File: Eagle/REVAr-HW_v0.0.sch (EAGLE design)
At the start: 74 parts, among them IC1 MC33269ST-5.0T3, IC2 MC33269D-5.0, IC3 ATMEGA2560-16AU, IC4 ATMEGA8U2-MU, IC5 LM358D, IC6 LP2985-33DBVR, Q1 16MHz, Q2 16MHz, T2 FDN340P, X1 DC21MMX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

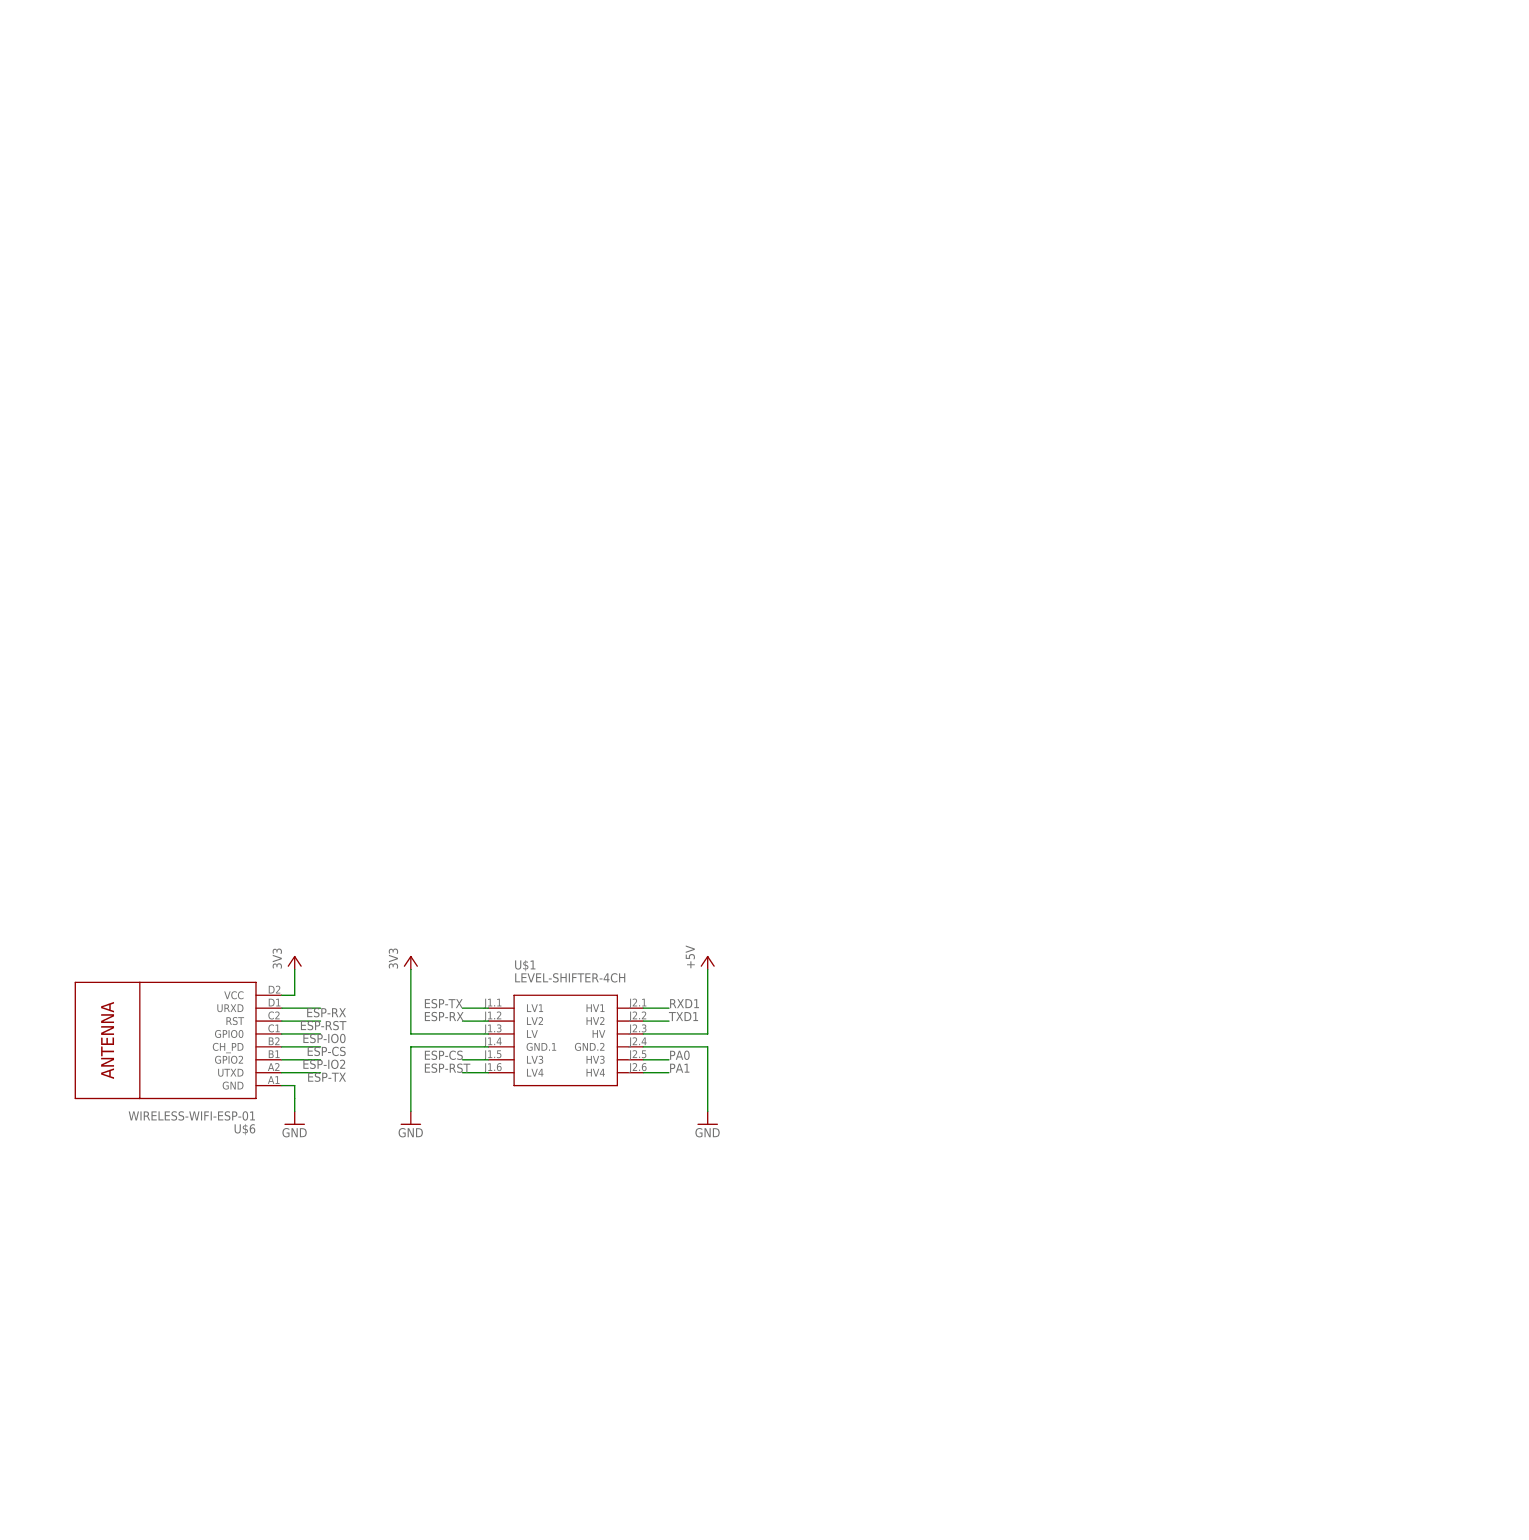
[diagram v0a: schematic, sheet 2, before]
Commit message: [HW] Add SPEC gas sensors and communication via RS485 with Arduino
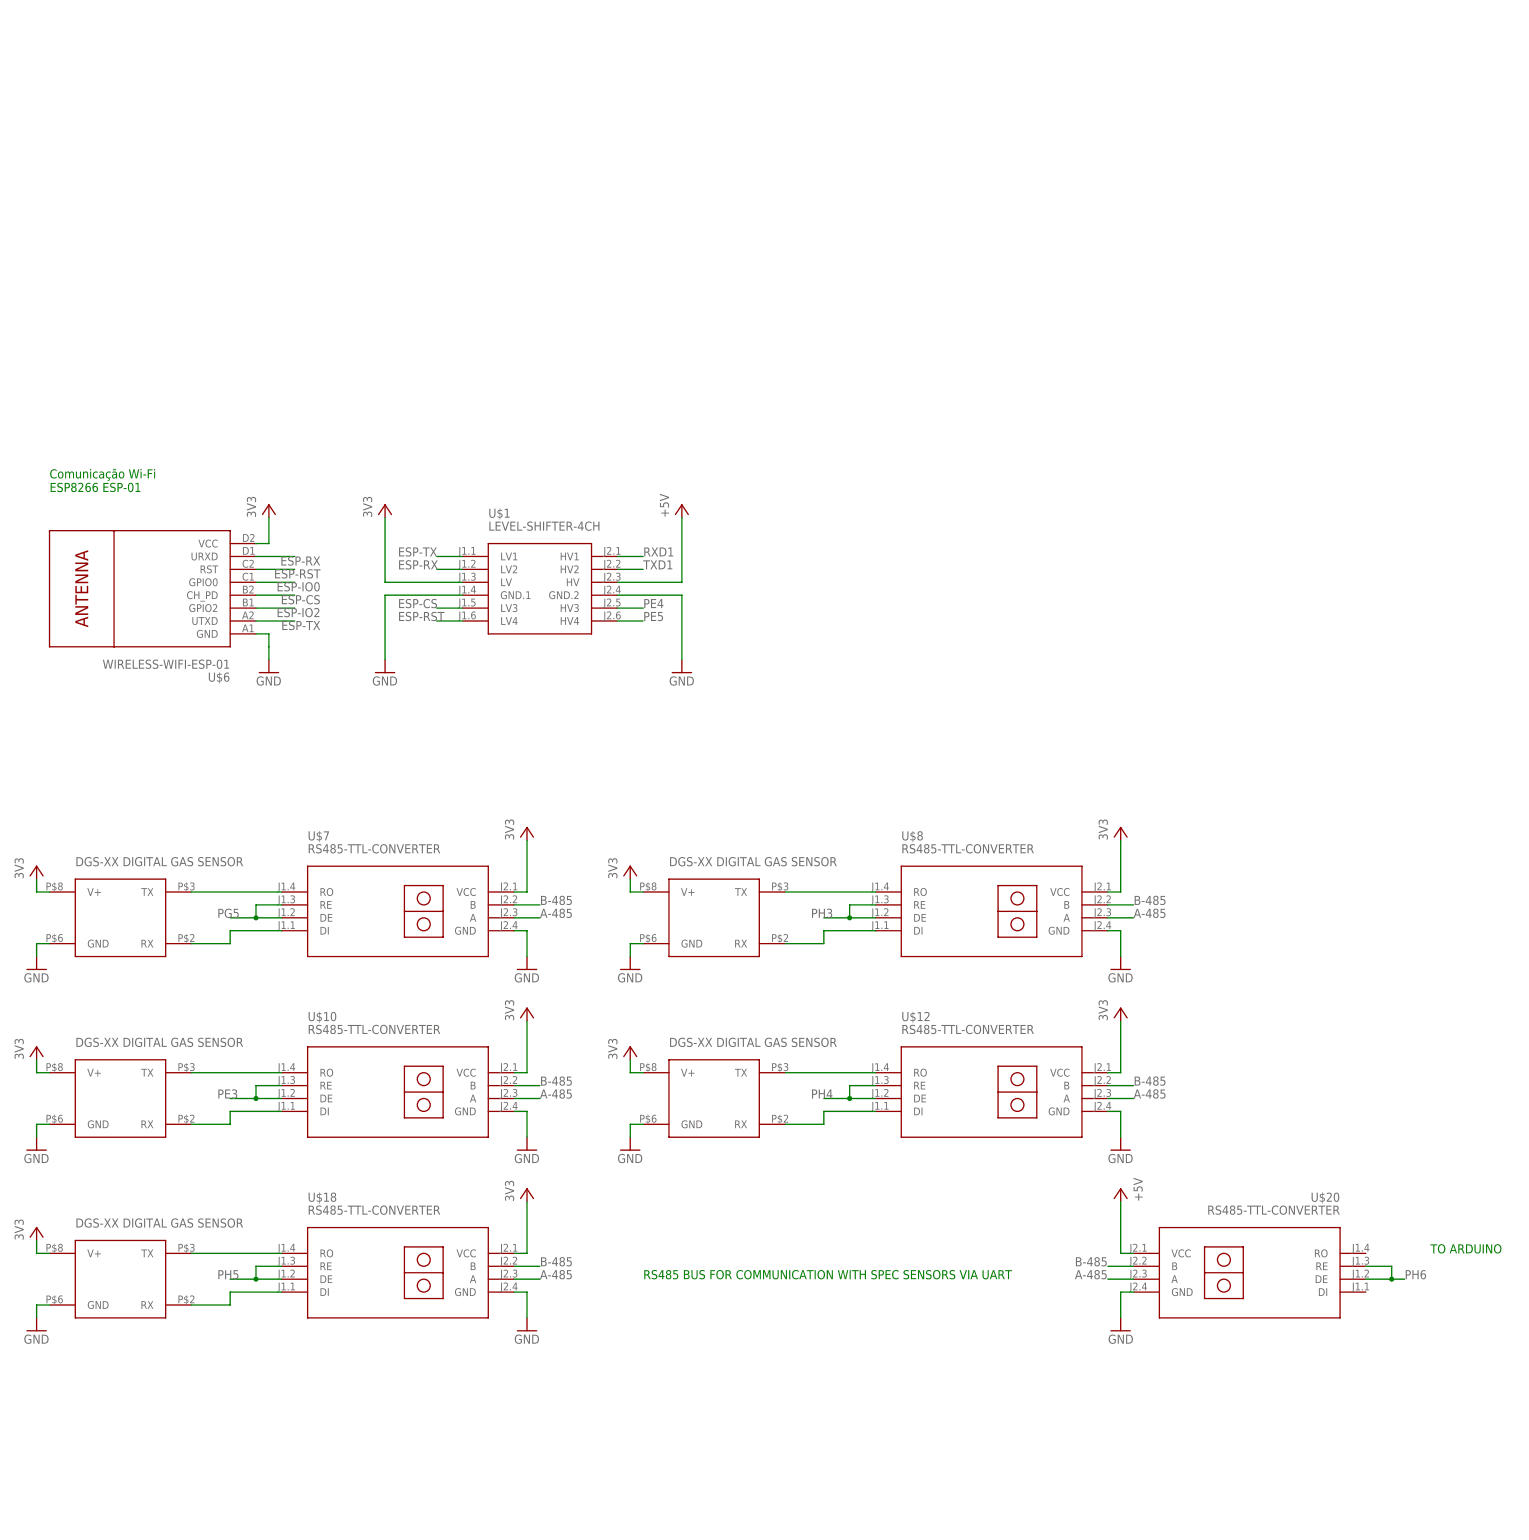
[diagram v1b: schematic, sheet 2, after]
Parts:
- added U$10, U$12, U$18, U$20, U$7, U$8: RS485-TTL-CONVERTER, diy-modules:RS485-TTL-CONVERTER
- added U$11, U$13, U$14, U$15, U$16, U$17, U$19, U$9: (no value), spec-sensors:DGS-XX
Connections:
- new net A-485: U$10.A, U$12.A, U$18.A, U$20.A, U$7.A, U$8.A
- new net B-485: U$10.B, U$12.B, U$18.B, U$20.B, U$7.B, U$8.B
- new net N$1: U$16.TX, U$7.RO
- new net N$10: U$12.DI, U$17.RX
- new net N$11: U$18.RO, U$19.TX
- new net N$12: U$18.DI, U$19.RX
- new net N$4: U$16.RX, U$7.DI
- new net N$5: U$10.RO, U$11.TX
- new net N$6: U$10.DI, U$11.RX
- new net N$7: U$8.RO, U$9.TX
- new net N$8: U$8.DI, U$9.RX
- new net N$9: U$12.RO, U$17.TX
- net GND: now also U$10.GND, U$11.GND, U$12.GND, U$16.GND, U$17.GND, U$18.GND, U$19.GND, U$20.GND, U$7.GND, U$8.GND, U$9.GND
- net PA0: no longer U$1.HV3
- net PA1: no longer U$1.HV4
- net PE3: now also U$10.DE, U$10.RE
- net PE4: now also U$1.HV3
- net PE5: now also U$1.HV4
- net PG5: now also U$7.DE, U$7.RE
- net PH3: now also U$8.DE, U$8.RE
- net PH4: now also U$12.DE, U$12.RE
- net PH5: now also U$18.DE, U$18.RE
- net PH6: now also U$20.DE, U$20.RE
- net VCC: now also U$10.VCC, U$11.V+, U$12.VCC, U$16.V+, U$17.V+, U$18.VCC, U$19.V+, U$20.VCC, U$7.VCC, U$8.VCC, U$9.V+
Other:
- note added: "Comunicação Wi-Fi ESP8266 ESP-01"
- note added: "RS485 BUS FOR COMMUNICATION WITH SPEC SENSORS VIA UART"
- note added: "TO ARDUINO"
- moved on the sheet: U$1, U$6

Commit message: [HW] Add PM UART sensor SDS011 to design
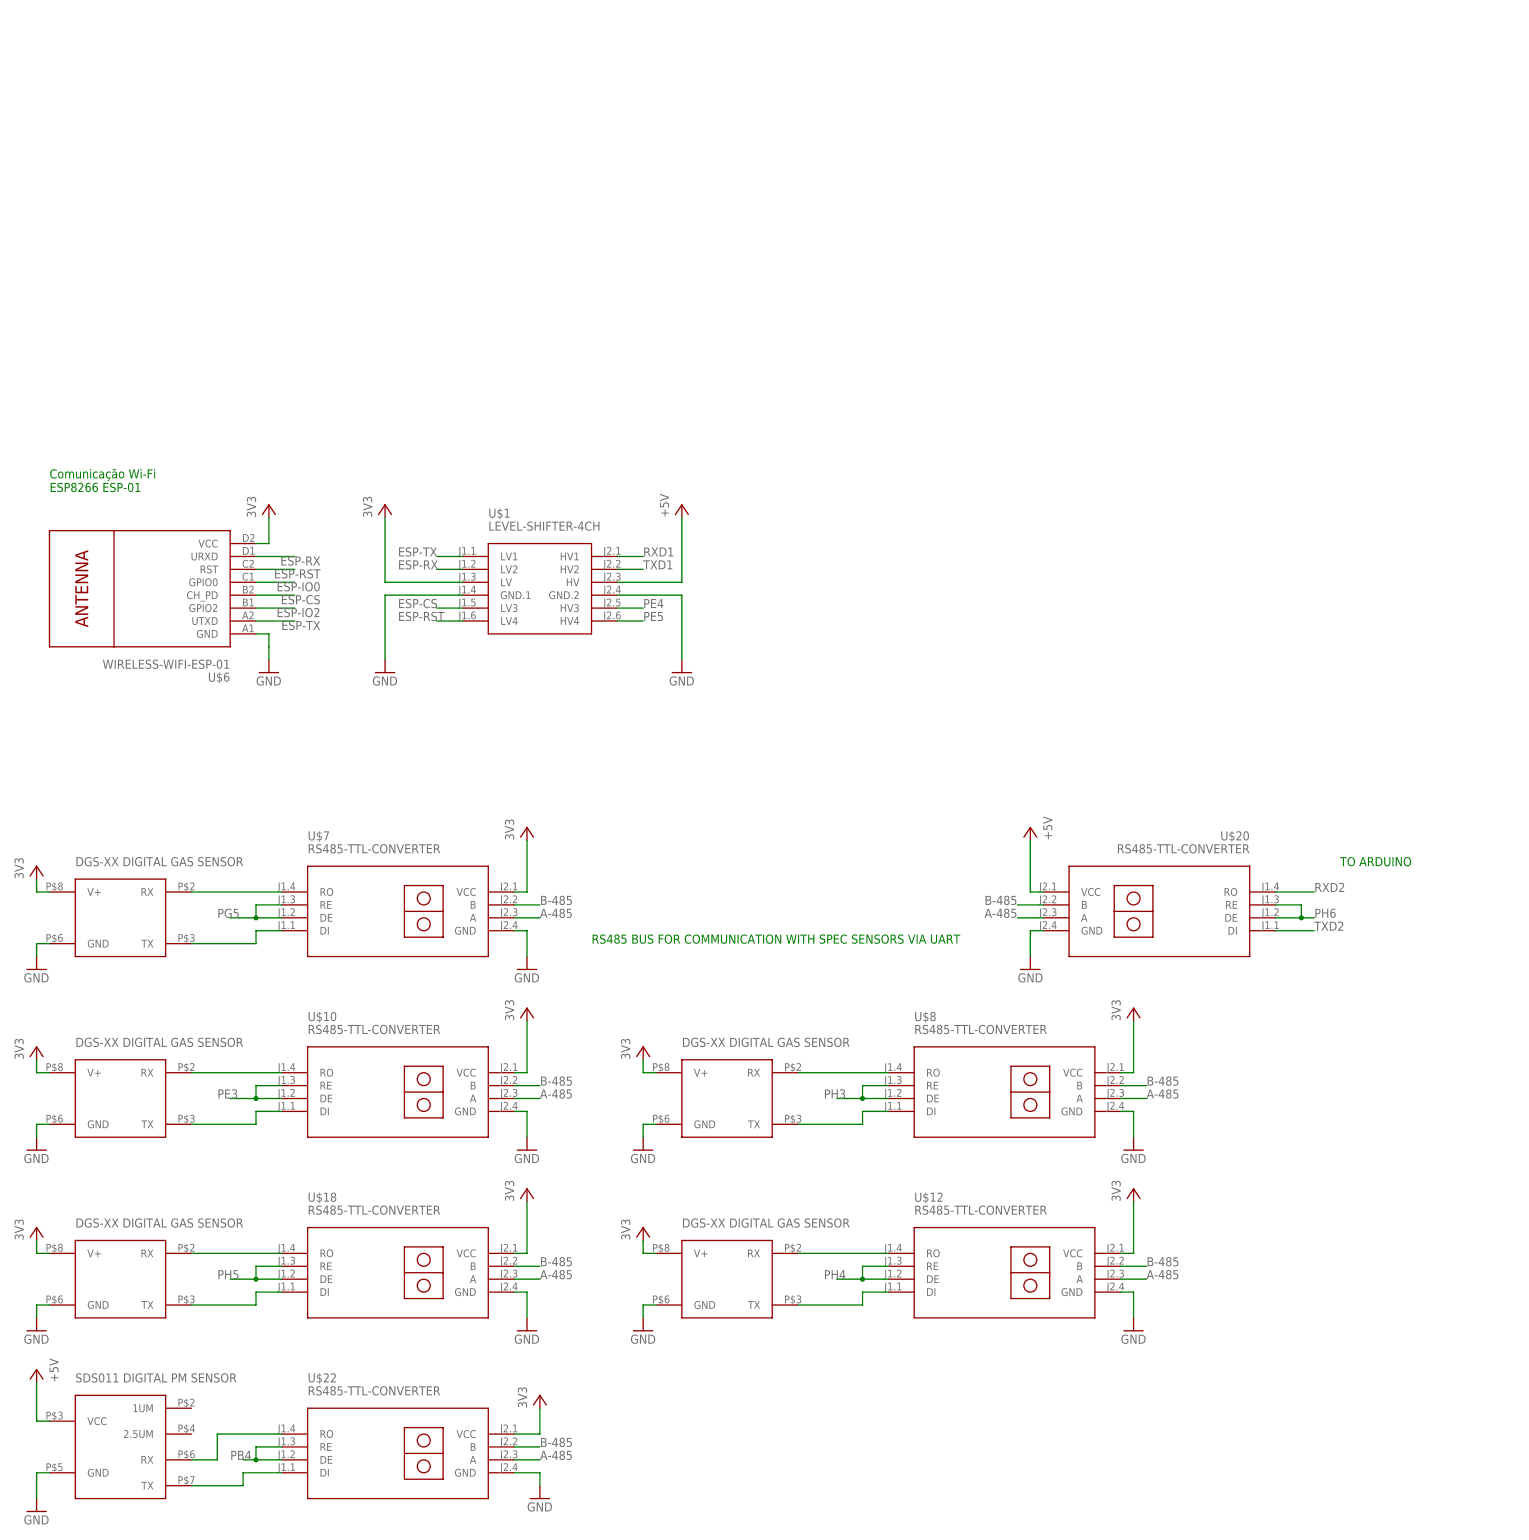
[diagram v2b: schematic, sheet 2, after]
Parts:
- removed U$13, U$14, U$15: (no value), spec-sensors:DGS-XX
- added U$21: SDS011, gas-sensors:SDS011
- added U$22: RS485-TTL-CONVERTER, diy-modules:RS485-TTL-CONVERTER
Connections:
- new net N$13: U$21.RX, U$22.RO
- new net N$14: U$21.TX, U$22.DI
- net A-485: now also U$22.A
- net B-485: now also U$22.B
- net GND: now also U$21.GND, U$22.GND
- net N$1: now also U$16.RX; no longer U$16.TX
- net N$10: now also U$12.RO; no longer U$12.DI
- net N$11: now also U$8.RO, U$9.RX; no longer U$18.RO, U$19.TX
- net N$12: now also U$12.DI, U$17.TX; no longer U$18.DI, U$19.RX
- net N$4: now also U$16.TX; no longer U$16.RX
- net N$5: now also U$11.RX; no longer U$11.TX
- net N$6: now also U$11.TX; no longer U$11.RX
- net N$7: now also U$18.RO, U$19.RX; no longer U$8.RO, U$9.TX
- net N$8: now also U$9.TX; no longer U$9.RX
- net N$9: now also U$18.DI, U$19.TX; no longer U$12.RO, U$17.TX
- net PB4: now also U$22.DE, U$22.RE
- net RXD2: now also U$20.RO
- net TXD2: now also U$20.DI
- net VCC: now also U$21.VCC, U$22.VCC
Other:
- moved on the sheet: U$12, U$20, U$8
